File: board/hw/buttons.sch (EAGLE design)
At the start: 11 parts

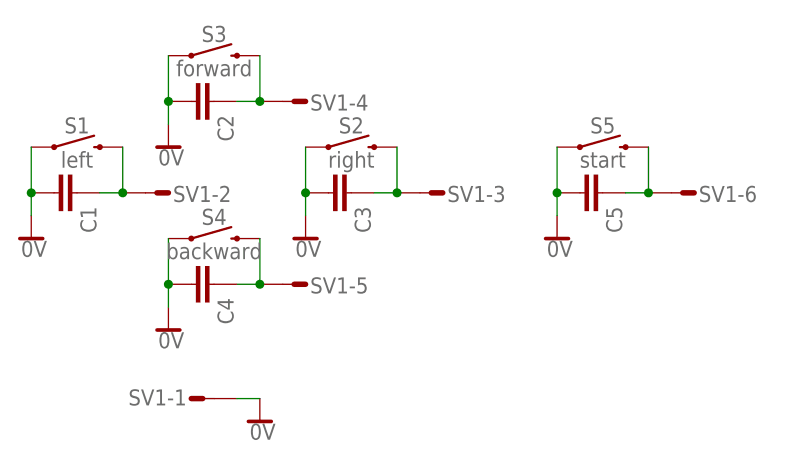
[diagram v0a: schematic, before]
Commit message: added 10nF to button boards capacitors
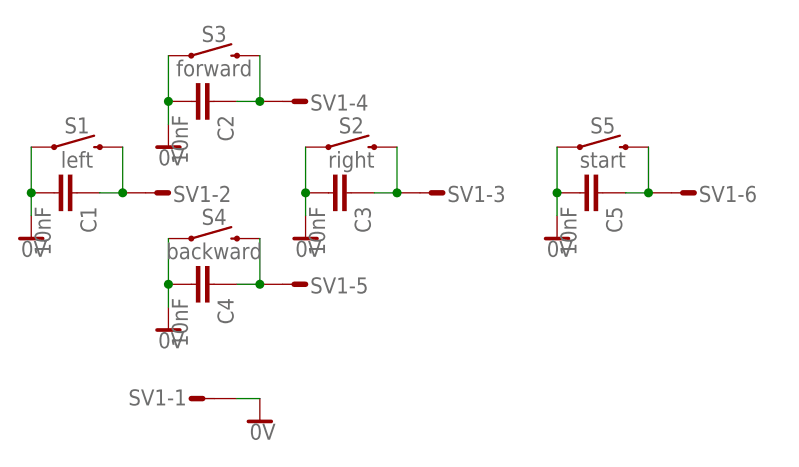
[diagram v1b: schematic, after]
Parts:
- C1, C2, C3, C4, C5: value (none) -> 10nF
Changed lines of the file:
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@@
 <part name="SV1" library="con-amp-mt" deviceset="S06P" device=""/>
 <part name="SUPPLY6" library="supply2" deviceset="0V" device=""/>
-<part name="C1" library="rcl" deviceset="C-EU" device="C0805K"/>
-<part name="C2" library="rcl" deviceset="C-EU" device="C0805K"/>
-<part name="C3" library="rcl" deviceset="C-EU" device="C0805K"/>
-<part name="C4" library="rcl" deviceset="C-EU" device="C0805K"/>
-<part name="C5" library="rcl" deviceset="C-EU" device="C0805K"/>
+<part name="C1" library="rcl" deviceset="C-EU" device="C0805K" value="10nF"/>
+<part name="C2" library="rcl" deviceset="C-EU" device="C0805K" value="10nF"/>
+<part name="C3" library="rcl" deviceset="C-EU" device="C0805K" value="10nF"/>
+<part name="C4" library="rcl" deviceset="C-EU" device="C0805K" value="10nF"/>
+<part name="C5" library="rcl" deviceset="C-EU" device="C0805K" value="10nF"/>
 </parts>
 <sheets>
